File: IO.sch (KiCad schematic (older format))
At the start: 0 parts

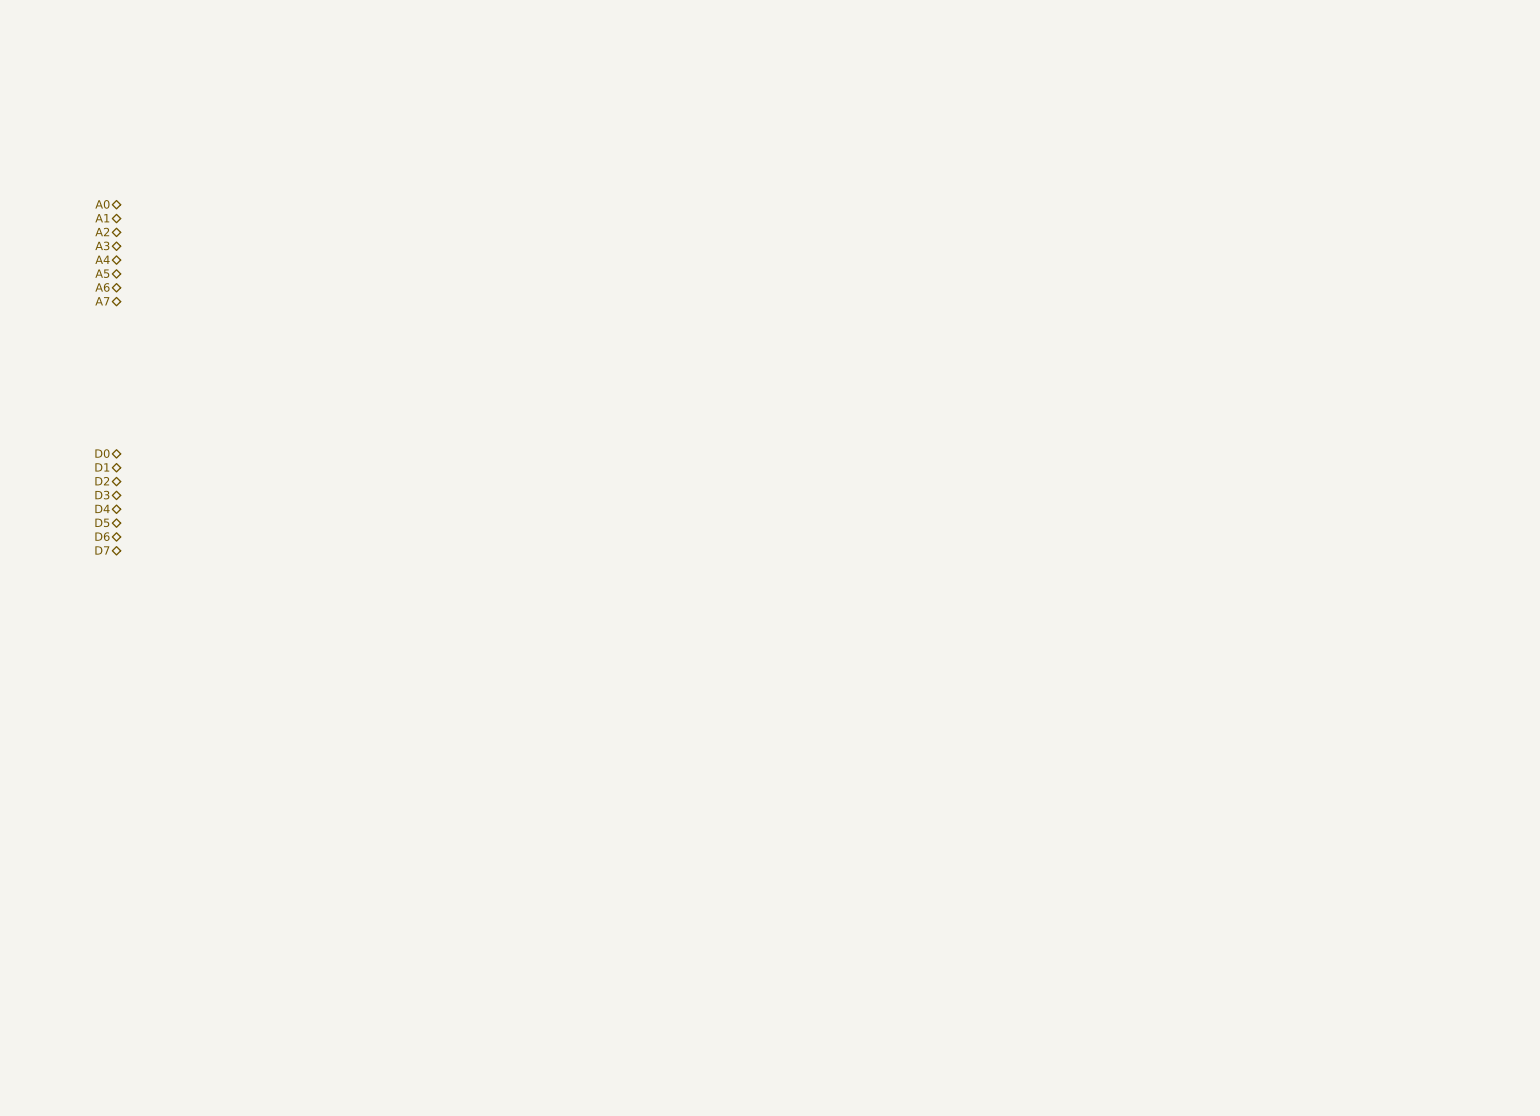
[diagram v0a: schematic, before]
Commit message: Added IO address decoder, 8 IO slots, partial IO bus buffering. Still to decide: what to do with all the /INT pins? TODO: add bi-directional data bus buffering (2x 74AC241?) for IO boards. This thing is turning into a monster :)
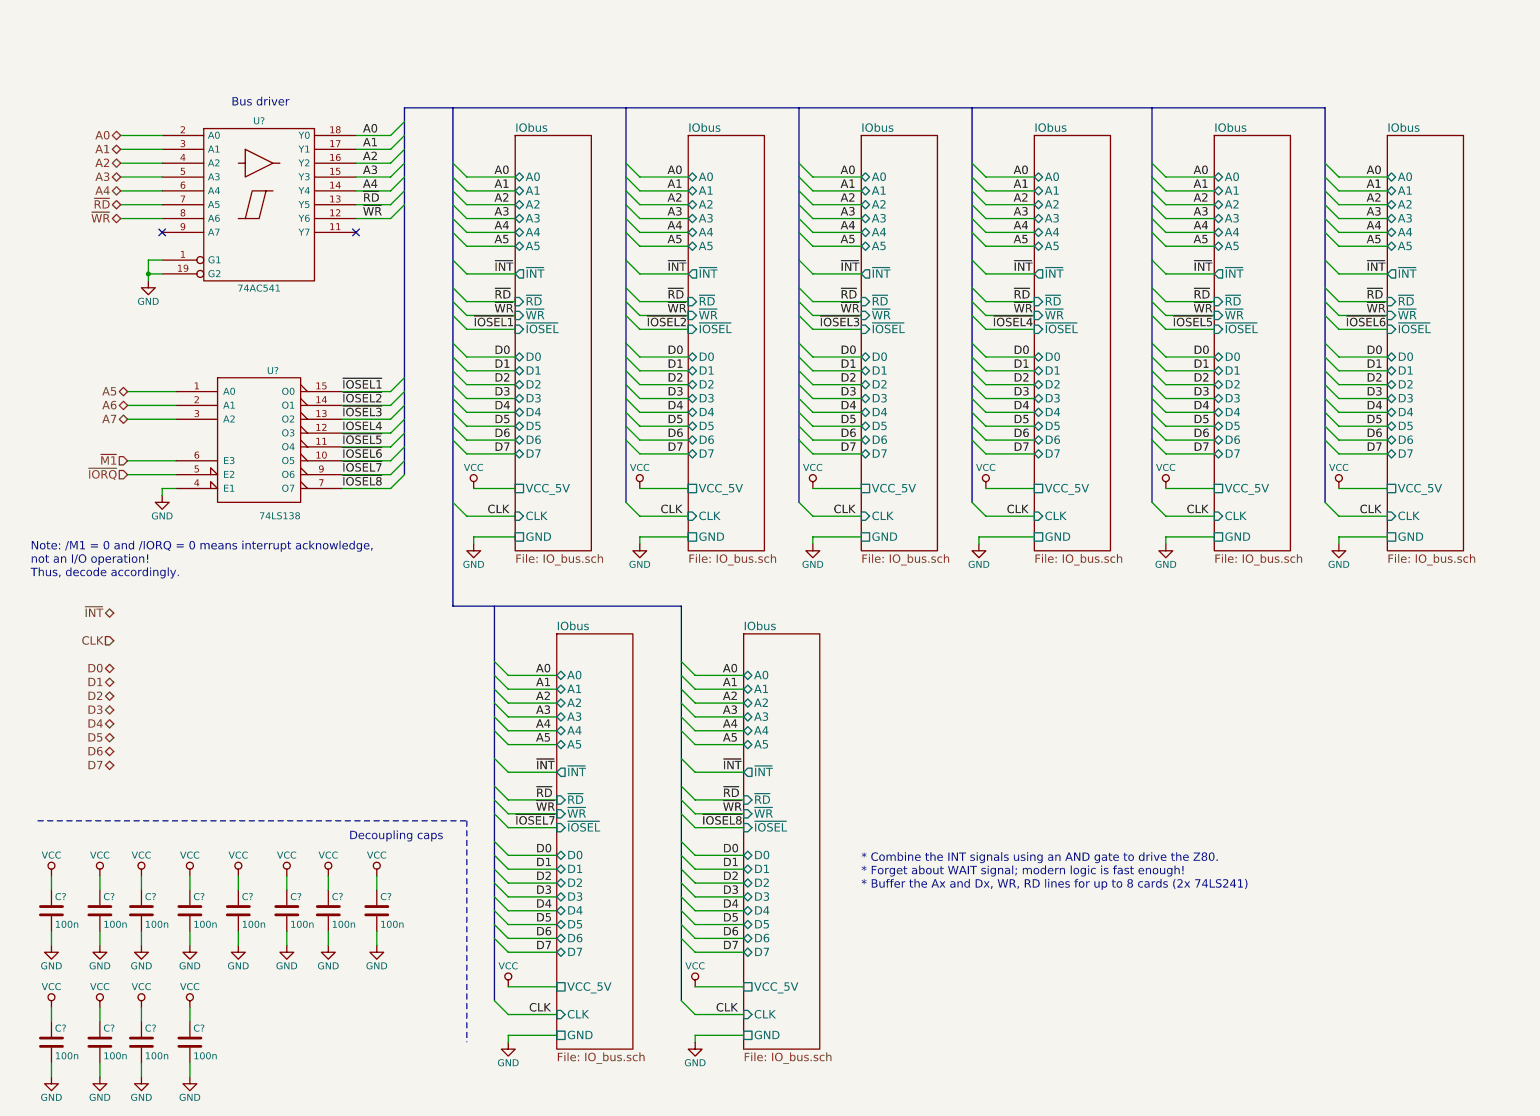
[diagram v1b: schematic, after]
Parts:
- added C? (x12): 100n, symbol C
- added U?: 74LS138, symbol 74LS138
- added U?: 74AC541, symbol 74LS541
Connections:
- net A0: now also U?.18 (Y0), U?.2 (A0)
- net A1: now also U?.17 (Y1), U?.3 (A1)
- net A2: now also U?.16 (Y2), U?.4 (A2)
- net A3: now also U?.15 (Y3), U?.5 (A3)
- net A4: now also U?.14 (Y4), U?.6 (A4)
- net A5: now also U?.1 (A0)
- net A6: now also U?.2 (A1)
- net A7: now also U?.3 (A2)
- new net GND: C?.2, C?.2, C?.2, C?.2, C?.2, C?.2, C?.2, C?.2, C?.2, C?.2, C?.2, C?.2, U?.1 (G1), U?.10 (GND), U?.19 (G2), U?.4 (E1), U?.8 (GND)
- new net IOSEL4: U?.12 (O3)
- new net VCC: C?.1, C?.1, C?.1, C?.1, C?.1, C?.1, C?.1, C?.1, C?.1, C?.1, C?.1, C?.1, U?.16 (VCC), U?.20 (VCC)
- new net ~IORQ: U?.5 (E2)
- new net ~IOSEL1: U?.15 (O0)
- new net ~IOSEL2: U?.14 (O1)
- new net ~IOSEL3: U?.13 (O2)
- new net ~IOSEL5: U?.11 (O4)
- new net ~IOSEL6: U?.10 (O5)
- new net ~IOSEL7: U?.9 (O6)
- new net ~IOSEL8: U?.7 (O7)
- new net ~M1: U?.6 (E3)
- new net ~RD: U?.13 (Y5), U?.7 (A5)
- new net ~WR: U?.12 (Y6), U?.8 (A6)
- no-connect marks 0 -> 2
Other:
- note added: "* Combine the INT signals using an AND gate to drive the Z80.\n* Forget about WAIT signal; modern logic is fast enough!\n* Buffer the Ax and Dx, WR, RD lines for up to 8 cards (2x 74LS241)"
- note added: "Bus driver"
- note added: "Decoupling caps"
- note added: "Note: /M1 = 0 and /IORQ = 0 means interrupt acknowledge, \nnot an I/O operation! \nThus, decode accordingly."

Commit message: Added missing signals to IO and added buffer
I've removed the /WAIT and also added a somewhat dodgy diode AND to
handle the bi-directional Dx buffer. Might work, might not.

Also cleaned up the buses and just tidied things up.
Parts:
- removed C? (x10): 100n, symbol C
- added C? (x3): 100n, symbol C
- added D? (x2): D, symbol D
- added R?: 10K, symbol R
- added U2: 74HC245, symbol 74HC245
- added U? (x2): 74LS21, symbol 74LS21
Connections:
- net labels added: ~CLK, ~RESET
- net labels removed: CLK
- wire segments 232 -> 243
- no-connect marks 2 -> 0
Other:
- note added: "* Dodgy diode AND, might work?"
- note added: "Note: /M1 = 0 and /IORQ = 0 means interrupt \nacknowledge, not an I/O operation! \nThus, decode accordingly."
- note removed: "Note: /M1 = 0 and /IORQ = 0 means interrupt acknowledge, \nnot an I/O operation! \nThus, decode accordingly."
- moved on the sheet: C?, U?

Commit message: Added /intack signal and a pri-encoder for /iosel
Brain fart on the diode crap. Was tired. Added a priority encoder to
enable the Dx buffer so it properly tristates when no IObus ports are
selected.

Added a NOR gate to provide a /intack signal for any board to properly
detect their interupt has been accepted but the z80. Boards will need to
figure out who the interupt is for.

Will have to add interupt priority pins to the boards to allow the
boards to put jump vectors onto the data bus to service the interrupt
This should be fairly easy, just means the service pritority of the
slots will be A-H, with A being the highest priority and H being the
lowest.

Going to replace the hex inverters with the spare NOR gates too.
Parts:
- removed C?: 100n, symbol C
- removed D? (x2): D, symbol D
- removed R?: 10K, symbol R
- removed U? (x2): 74LS21, symbol 74LS21
- added D? (x4): LED, symbol LED
- added R? (x4): R, symbol R
- added U?: 74LS148, symbol 74LS148
- added U?: 74HC02, symbol 74HC02
- C6, C7, C8, C9: renamed from C?; footprint (none) -> Capacitors_SMD:C_0805_HandSoldering
- U3: renamed from U?; footprint (none) -> Housings_DIP:DIP-20_W7.62mm_LongPads
- U4: renamed from U?; footprint (none) -> Housings_DIP:DIP-16_W7.62mm_LongPads
- U5: renamed from U2; footprint (none) -> Housings_DIP:DIP-20_W7.62mm_LongPads
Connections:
- net labels added: A0-B, A1-B, A2-B, A3-B, A4-B, A5-B, D0-B, D1-B, D2-B, D3-B, D4-B, D5-B, D6-B, D7-B, S-LED0, S-LED1, S-LED2, ~BUS_EN, ~CLK-B, ~INTACK, ~RD-B, ~WR-B
- net labels removed: IOSEL4
- wire segments 243 -> 265
- no-connect marks 0 -> 1
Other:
- note added: "Note: Priority encoder controls \nthe tri-state of the Dx buffer.\nNo IOSEL, buffer tri-stated."
- note added: "Status LED to show\nan IObus is selected"
- note removed: "* Dodgy diode AND, might work?"
- note removed: "Note: /M1 = 0 and /IORQ = 0 means interrupt \nacknowledge, not an I/O operation! \nThus, decode accordingly."
- moved on the sheet: U3, U4, U5

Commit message: Added interrupt priority pins to bus
These pins allow the boards to accept an interrupt assert priority of
the recieved interrupt ACK and load the data bus with a jump offset to
an ISR. Once a board has assert priority it sets it's IEO low so all
lower priority boards know the interrupt ACK wasn't for them and to try
again.

This will be a beast!
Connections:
- net labels added: INT-A, INT-AB, INT-BC, INT-CD, INT-DE, INT-EF, INT-FG, INT-GH
- wire segments 265 -> 281
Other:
- note added: "/M1 and /IORQ active, an \ninterrupt has been ACKd"
- note added: "Addr Decode and Interrupt"
- note added: "Data bus driver"
- note added: "INT-A set high to start the interrupt priority chain. A highest, H lowest"
- note removed: "* Combine the INT signals using an AND gate to drive the Z80.\n* Forget about WAIT signal; modern logic is fast enough!\n* Buffer the Ax and Dx, WR, RD lines for up to 8 cards (2x 74LS241)"
- moved on the sheet: U5

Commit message: Removed the interrupt priority circuitry
After second thought the added complexity just wasn't worth it.
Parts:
- removed U?: 74HC02, symbol 74HC02
- gave numbers to parts that had none: 9
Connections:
- net labels removed: INT-A, INT-AB, INT-BC, INT-CD, INT-DE, INT-EF, INT-FG, INT-GH, ~INTACK
- wire segments 281 -> 253
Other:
- note removed: "/M1 and /IORQ active, an \ninterrupt has been ACKd"
- note removed: "INT-A set high to start the interrupt priority chain. A highest, H lowest"
- moved on the sheet: C6, C7, C8, C9, D1, D3, D4, D5, R1, R15, R16, R6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
